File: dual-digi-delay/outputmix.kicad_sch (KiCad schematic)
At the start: 16 parts, among them U1 TL072

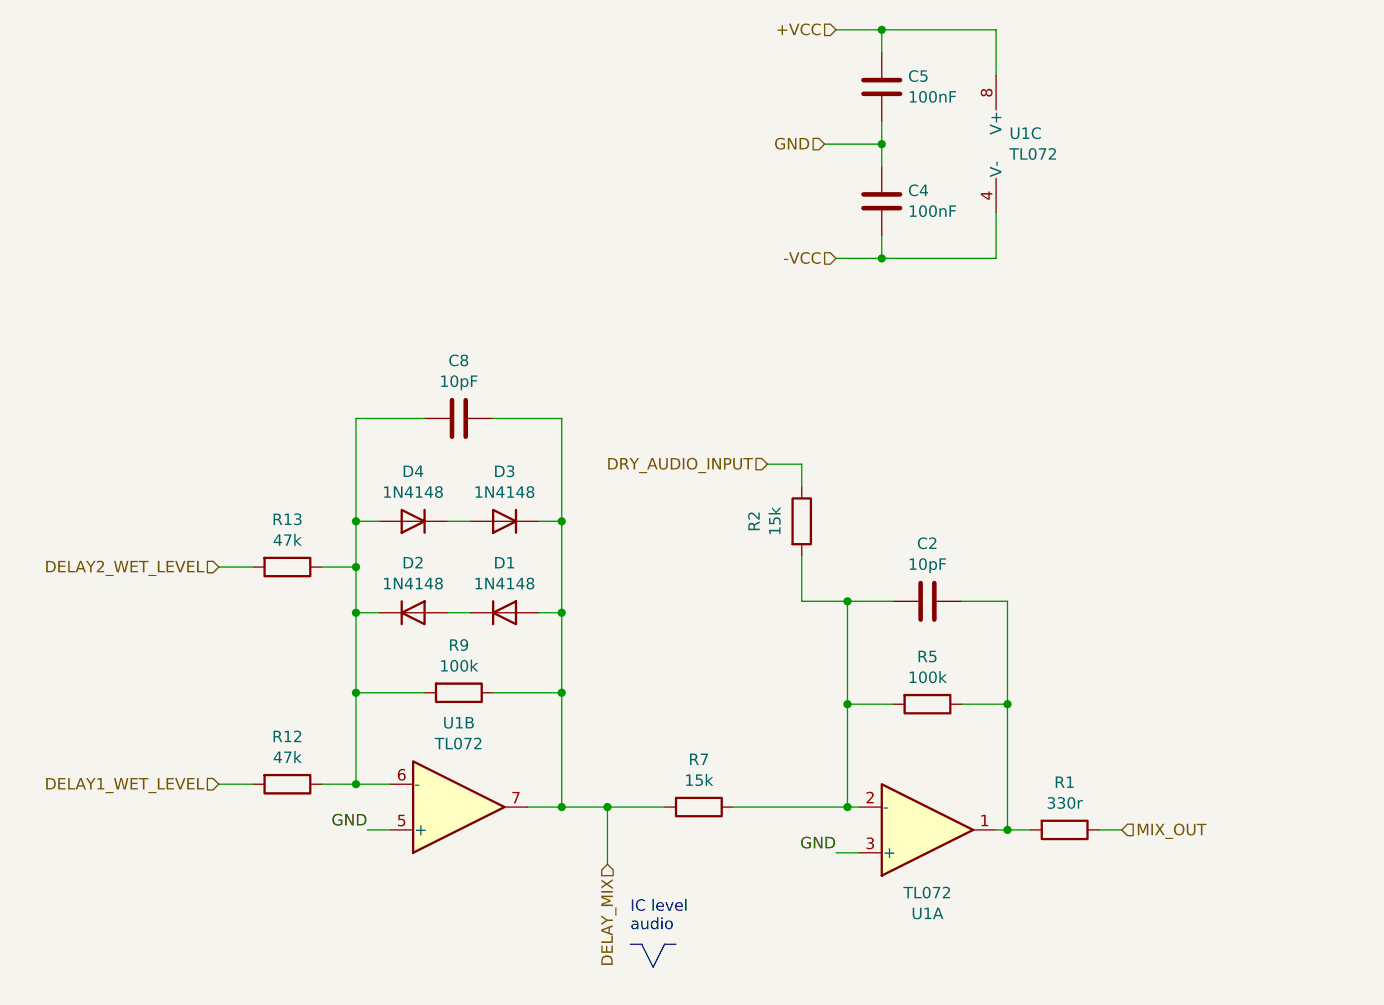
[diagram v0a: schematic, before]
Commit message: Making temporary branch for rev2 builds
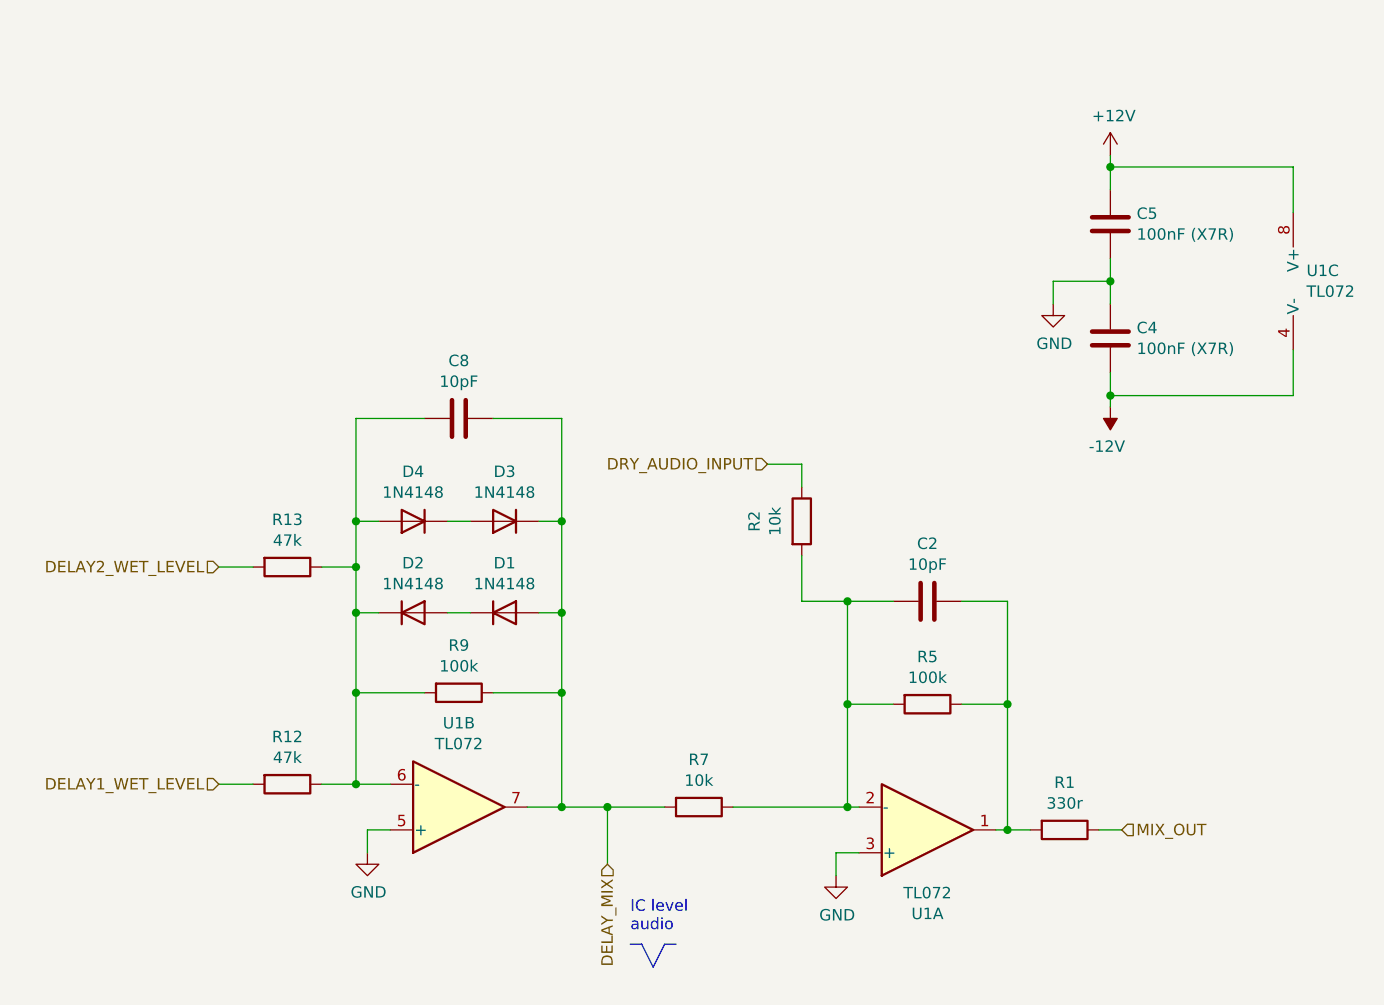
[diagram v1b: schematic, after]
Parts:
- C4, C5: value 100nF -> 100nF (X7R)
- R2, R7: value 15k -> 10k
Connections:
- net +VCC renamed +12V
- net -VCC renamed -12V
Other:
- moved on the sheet: C4, C5, U1C
